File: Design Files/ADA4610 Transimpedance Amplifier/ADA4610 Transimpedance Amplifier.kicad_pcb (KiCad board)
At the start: 2 copper layers, 33 parts, among them J1 Conn_01x03_Male, J2 Conn_Coaxial, U1 ADA4610-1xR, U2 ADA4610-1xR

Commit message: Initial Placement Done.
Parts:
- C1, C2, C3, C4, C5, C6, C7, J1, J2, R1, R10, R2, R3, R4, R5, R6, R7, R8, R9: moved to B.Cu
- D1: footprint Package_TO_SOT_THT:TO-18-2_Lens -> ADA4610-transimpedance-amplifier:TO-18-2_Lens_Centered
- TP1, TP4: value TestPoint -> TP_GND; moved to B.Cu
- TP2: value TestPoint -> TP_V+; moved to B.Cu
- TP3: value TestPoint -> TP_V-; moved to B.Cu
- TP5: value TestPoint -> TP_TIA_OUT; moved to B.Cu
- TP6: value TestPoint -> TP_OUTPUT; moved to B.Cu
- TP7: value TestPoint -> TP_OUTPUT_50OHM; moved to B.Cu
- U1, U2: footprint Package_TO_SOT_SMD:SOT-23-5_HandSoldering -> Package_TO_SOT_SMD:SOT-23-5; moved to B.Cu
- moved TP1 104.6 mm to (134.9, 72.4), turned to 180 degrees
- moved C4 102.3 mm to (104.8, 73.7), turned to 180 degrees
- moved TP3 99.1 mm to (127.2, 82.5), turned to 180 degrees
- moved R9 95.7 mm to (94.0, 71.8), turned to -90 degrees
- moved R3 94.6 mm to (114.3, 76.2), turned to 90 degrees
- moved C1 92.2 mm to (107.3, 67.3), turned to 90 degrees
- moved R10 90.3 mm to (85.1, 71.1), turned to -90 degrees
- moved C2 88.2 mm to (116.2, 76.2), turned to 90 degrees
- moved U2 87.8 mm to (92.7, 76.2), turned to 180 degrees
- moved C3 87.3 mm to (115.6, 72.4), turned to 180 degrees
- moved TP5 86.4 mm to (101.6, 69.8)
- moved C6 85.9 mm to (89.5, 73.0)
- moved R5 82.1 mm to (110.5, 76.2), turned to -90 degrees
- moved J1 81.5 mm to (134.9, 85.1), turned to 90 degrees
- moved C5 80.7 mm to (89.5, 69.2), turned to 180 degrees
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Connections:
- U1 pad 1: unconnected-(U1-Pad1) -> Net-(C4-Pad2)
- U1 pad 2: Net-(C4-Pad1) -> VEE
- U1 pad 4: VEE -> Net-(C4-Pad1)
- U1 pad 5: unconnected-(U1-Pad5) -> VCC
- U2 pad 1: unconnected-(U2-Pad1) -> Net-(R8-Pad1)
- U2 pad 2: Net-(R7-Pad2) -> VEE
- U2 pad 4: VEE -> Net-(R7-Pad2)
- U2 pad 5: unconnected-(U2-Pad5) -> VCC
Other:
- board outline added: 63.5 x 63.5 mm

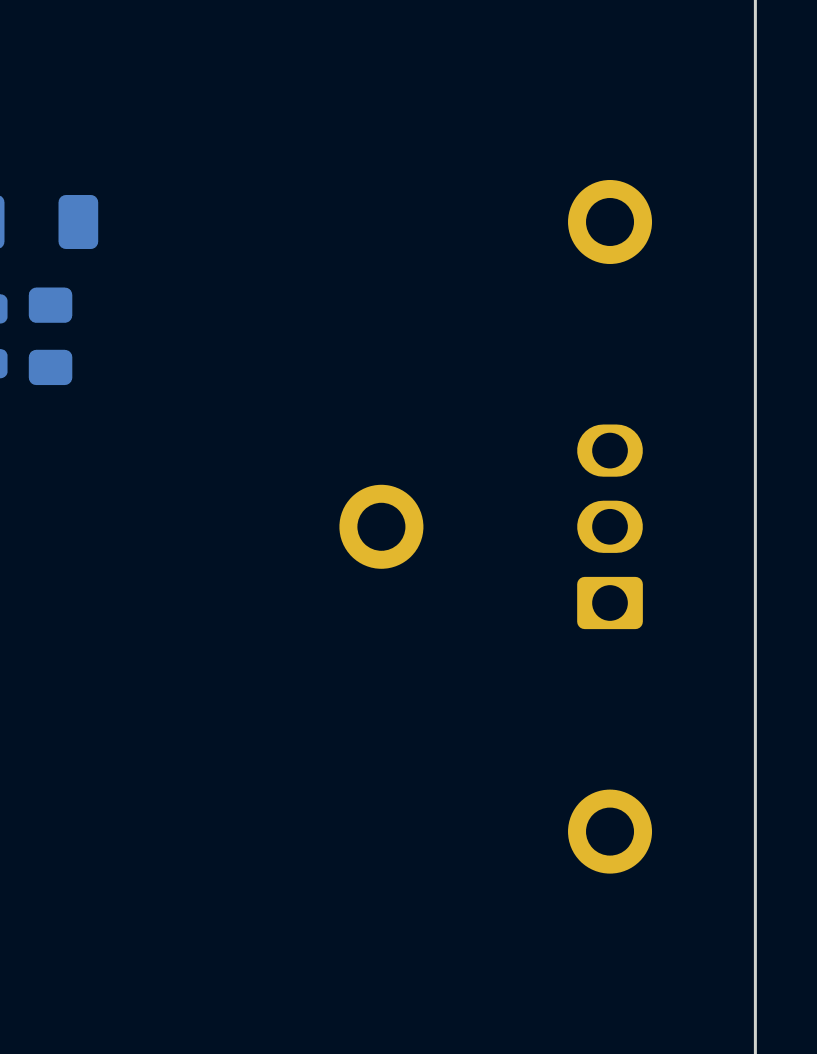
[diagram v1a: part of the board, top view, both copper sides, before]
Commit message: Placement and text completed.
Ready for traces.
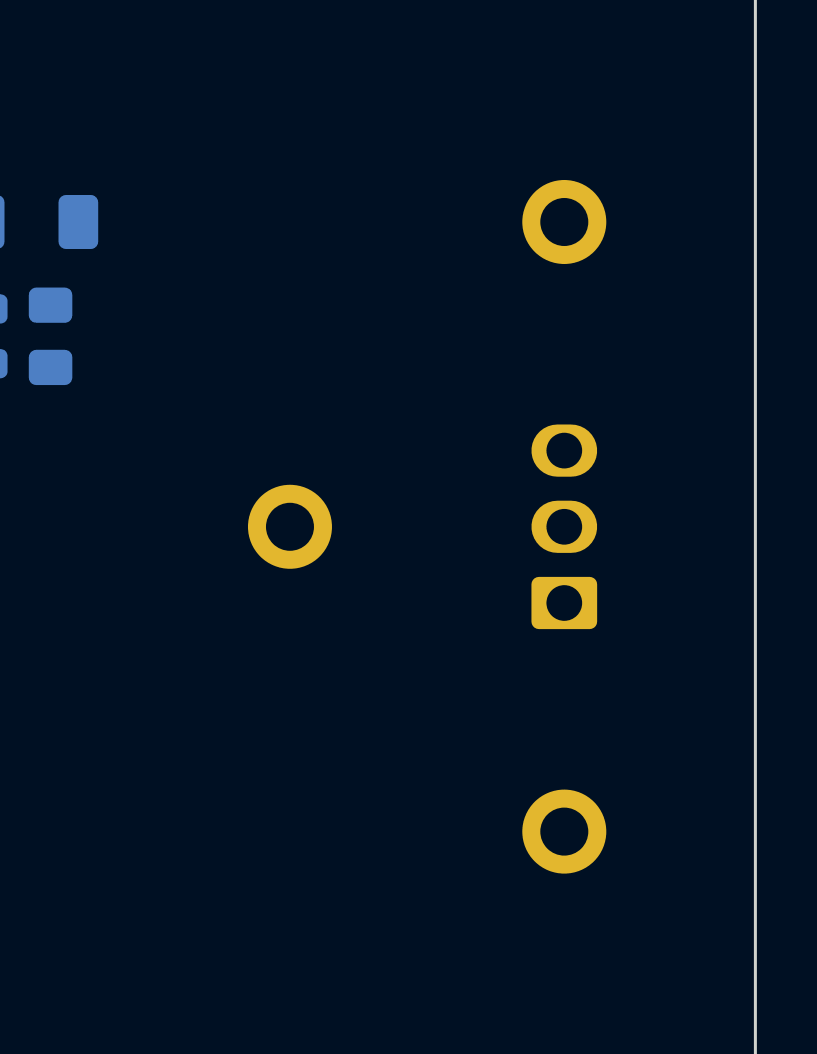
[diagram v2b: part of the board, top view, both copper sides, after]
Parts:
- moved TP3 3.05 mm to (124.2, 82.5)
- moved J1 1.52 mm to (133.3, 85.1)
- moved TP1 1.52 mm to (133.3, 72.4)
- moved TP2 1.52 mm to (133.3, 92.7)
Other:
- board text added: "ADA4610-1 TRANSIMPEDANCE AMPLIFIER BRENTON SALMI, KB1LQD AUGUST 2022, REV 1.0"
- board text added: "GND"
- board text added: "TP_GND"
- board text added: "TP_OUTPUT"
- board text added: "TP_OUT_50-OHM"
- board text added: "TP_TIA_OUT"
- board text added: "TP_V+"
- board text added: "TP_V-"
- board text added: "V+"
- board text added: "V-"
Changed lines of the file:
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@@
   )
   (footprint "TestPoint:TestPoint_Keystone_5010-5014_Multipurpose" (layer "B.Cu")
-    (at 134.854 92.71 180)
+    (at 133.33 92.71 180)
     (descr "Keystone Miniature THM Test Point 5010-5014, http://www.keyelco.com/product-pdf.cfm?p=1319")
     (tags "Through Hole Mount Test Points")
@@
   )
   (footprint "TestPoint:TestPoint_Keystone_5010-5014_Multipurpose" (layer "B.Cu")
-    (at 127.234 82.55 180)
+    (at 124.186 82.55 180)
     (descr "Keystone Miniature THM Test Point 5010-5014, http://www.keyelco.com/product-pdf.cfm?p=1319")
     (tags "Through Hole Mount Test Points")
@@
   )
   (footprint "TestPoint:TestPoint_Keystone_5010-5014_Multipurpose" (layer "B.Cu")
-    (at 134.854 72.39 180)
+    (at 133.33 72.39 180)
     (descr "Keystone Miniature THM Test Point 5010-5014, http://www.keyelco.com/product-pdf.cfm?p=1319")
     (tags "Through Hole Mount Test Points")
@@
   )
   (footprint "Connector_Molex:Molex_KK-254_AE-6410-03A_1x03_P2.54mm_Vertical" (layer "B.Cu")
-    (at 134.854 85.09 90)
+    (at 133.33 85.09 90)
     (descr "Molex KK-254 Interconnect System, old/engineering part number: AE-6410-03A example for new part number: 22-27-2031, 3 Pins (http://www.molex.com/pdm_docs/sd/022272021_sd.pdf), generated with kicad-footprint-generator")
     (tags "connector Molex KK-254 vertical")
@@
   (gr_line (start 133.35 107.95) (end 129.54 103.505) (layer "User.4") (width 0.15))
   (gr_line (start 82.55 57.15) (end 133.35 107.95) (layer "User.4") (width 0.15))
+  (gr_text "TP_OUT_50-OHM" (at 78.74 67.945 270) (layer "B.SilkS")
+    (effects (font (size 1 1) (thickness 0.15) italic) (justify mirror))
+  )
+  (gr_text "TP_OUTPUT" (at 97.155 90.17 270) (layer "B.SilkS")
+    (effects (font (size 1 1) (thickness 0.15) italic) (justify mirror))
+  )
+  (gr_text "V+" (at 128.1176 85.09) (layer "B.SilkS")
+    (effects (font (size 1 1) (thickness 0.15) italic) (justify mirror))
+  )
+  (gr_text "TP_TIA_OUT" (at 101.6 62.865 270) (layer "B.SilkS")
+    (effects (font (size 1 1) (thickness 0.15) italic) (justify mirror))
+  )
+  (gr_text "TP_V+" (at 127.635 92.71) (layer "B.SilkS")
+    (effects (font (size 1 1) (thickness 0.15) italic) (justify mirror))
+  )
+  (gr_text "TP_V-" (at 118.745 82.55) (layer "B.SilkS")
+    (effects (font (size 1 1) (thickness 0.15) italic) (justify mirror))
+  )
+  (gr_text "GND" (at 128.27 80.01) (layer "B.SilkS")
+    (effects (font (size 1 1) (thickness 0.15) italic) (justify mirror))
+  )
+  (gr_text "ADA4610-1 TRANSIMPEDANCE AMPLIFIER\nBRENTON SALMI, KB1LQD\nAUGUST 2022, REV 1.0" (at 120.65 107.95) (layer "B.SilkS")
+    (effects (font (size 1 1) (thickness 0.15)) (justify left mirror))
+  )
+  (gr_text "TP_GND" (at 88.9 95.885 270) (layer "B.SilkS")
+    (effects (font (size 1 1) (thickness 0.15) italic) (justify mirror))
+  )
+  (gr_text "TP_GND" (at 127.635 72.39) (layer "B.SilkS")
+    (effects (font (size 1 1) (thickness 0.15) italic) (justify mirror))
+  )
+  (gr_text "V-" (at 128.27 82.55) (layer "B.SilkS")
+    (effects (font (size 1 1) (thickness 0.15) italic) (justify mirror))
+  )
 )

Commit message: Updated PCB to osh park 2 layer rules.
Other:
- rule pad_to_mask_clearance: 0 -> 0.0508
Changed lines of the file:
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@@
     (46 "B.CrtYd" user "B.Courtyard")
     (47 "F.CrtYd" user "F.Courtyard")
-    (48 "B.Fab" user)
-    (49 "F.Fab" user)
     (50 "User.1" user)
     (51 "User.2" user)
@@
       (dielectric_constraints no)
     )
-    (pad_to_mask_clearance 0)
+    (pad_to_mask_clearance 0.0508)
     (aux_axis_origin 82.55 107.95)
     (grid_origin 82.55 107.95)

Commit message: Board completed and no errors.
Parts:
- removed TP7: TP_OUTPUT_50OHM, TestPoint:TestPoint_Keystone_5010-5014_Multipurpose
- moved R10 4.32 mm to (85.1, 66.8), turned to 90 degrees
- moved C6 3.17 mm to (87.6, 75.6)
- moved C5 1.40 mm to (89.5, 67.8)
- turned C1 to -90 degrees
- turned C2 to -90 degrees
- turned R4 to 90 degrees
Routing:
- net Net-(C4-Pad2): track 0.00 -> 26.9 mm
- net Net-(C5-Pad2): track 0.00 -> 23.5 mm
- net VEE: track 0.00 -> 15.9 mm
- net Net-(R8-Pad1): track 0.00 -> 13.6 mm
- net VCC: track 0.00 -> 12.5 mm, vias 0 -> 20
- net Net-(C4-Pad1): track 0.00 -> 11.9 mm
- net GND: track 0.00 -> 10.5 mm, vias 0 -> 20
- net Net-(C2-Pad2): track 0.00 -> 10.1 mm
- net Net-(C5-Pad1): track 0.00 -> 5.37 mm
- net Net-(R7-Pad2): track 0.00 -> 4.37 mm
- net Net-(D1-Pad2): track 0.00 -> 4.17 mm
- added copper zone on B.Cu, net GND
- added copper zone on F.Cu, net GND
- added copper zone on B.Cu, net VCC
- added copper zone on F.Cu, net VCC
- added copper zone on B.Cu, net VEE
